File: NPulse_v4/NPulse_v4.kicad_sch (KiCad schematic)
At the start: 48 parts, among them IC1 TXU0202QDCUR, J2 Conn_01x04_Pin, J3 Conn_01x06_Pin, J4 Conn_01x04_Pin, Q1 PMOS, Q2 NMOS, SW1 SW_Push, SW2 SW_SPDT, U1 STM32G484METx, Y1 16MHz

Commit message: some modifications on the routing
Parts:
- H1: footprint MountingHole:MountingHole_3.2mm_M3 -> MountingHole:MountingHole_2.2mm_M2
- IC1: footprint TXU:SOP50P310X90-8N -> TXU0202:SOP50P310X90-8N
- SW1: footprint Button_Switch_SMD:SW_Push_1P1T_NO_CK_KSC7xxJ -> Button_Switch_SMD:SW_SPST_TL3305B
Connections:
- net AD_Vbat: now also U1.17 (PA3); no longer U1.13 (PA1)
- net ENC8_S1: now also U1.12 (PA0); no longer U1.14 (PA2)
- net ENC8_S2: now also U1.13 (PA1); no longer U1.17 (PA3)
- net LED: now also U1.14 (PA2); no longer U1.12 (PA0)
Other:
- note added: "Input"
- note added: "Tactile Button TL3305BF100QG MO: 612-TL3305BF100QG"
- note added: "Translateur TXU0202DCUR DK: 296-TXU0202DCURCT-ND MO: 595-TXU0202DCUR"
- note removed: "Translateur TXU0202DCUR DK: 296-TXU0202DCURCT-ND"
- note removed: "input"

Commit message: Udate mounting holes positions
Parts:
- added H2, H5: MountingHole, MountingHole:MountingHole_2.2mm_M2, symbol Mechanical:MountingHole
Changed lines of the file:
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@@
+	)
+	(symbol
+		(lib_id "Mechanical:MountingHole")
+		(at 129.54 185.42 0)
+		(unit 1)
+		(exclude_from_sim yes)
+		(in_bom no)
+		(on_board yes)
+		(dnp no)
+		(property "Reference" "H5"
+			(at 128.524 189.23 0)
+			(effects
+				(font
+					(size 1.27 1.27)
+				)
+				(justify left)
+			)
+		)
+		(property "Value" "MountingHole"
+			(at 132.08 186.6899 0)
+			(effects
+				(font
+					(size 1.27 1.27)
+				)
+				(justify left)
+				(hide yes)
+			)
+		)
+		(property "Footprint" "MountingHole:MountingHole_2.2mm_M2"
+			(at 129.54 185.42 0)
+			(effects
+				(font
+					(size 1.27 1.27)
+				)
+				(hide yes)
+			)
+		)
+		(property "Datasheet" "~"
+			(at 129.54 185.42 0)
+			(effects
+				(font
+					(size 1.27 1.27)
+				)
+				(hide yes)
+			)
+		)
+		(property "Description" "Mounting Hole without connection"
+			(at 129.54 185.42 0)
+			(effects
+				(font
+					(size 1.27 1.27)
+				)
+				(hide yes)
+			)
+		)
+		(instances
+			(project "NPulse_v4"
+				(path "/1b9ce217-75d5-40c4-b78f-f756c7214a1a"
+					(reference "H5")
+					(unit 1)
+				)
+			)
+		)
 	)
 	(symbol
@@
 					(unit 1)
 				)
+			)
+		)
+	)
+	(symbol
+		(lib_id "Mechanical:MountingHole")
+		(at 121.92 185.42 0)
+		(unit 1)
+		(exclude_from_sim yes)
+		(in_bom no)
+		(on_board yes)
+		(dnp no)
+		(property "Reference" "H2"
+			(at 121.158 189.23 0)
+			(effects
+				(font
+					(size 1.27 1.27)
+				)
+				(justify left)
+			)
+		)
+		(property "Value" "MountingHole"
+			(at 115.062 189.738 0)
+			(effects
+				(font
+					(size 1.27 1.27)
+				)
+				(justify left)
+				(hide yes)
+			)
+		)
+		(property "Footprint" "MountingHole:MountingHole_2.2mm_M2"
+			(at 121.92 185.42 0)
+			(effects
+				(font
+					(size 1.27 1.27)
+				)
+				(hide yes)
+			)
+		)
+		(property "Datasheet" "~"
+			(at 121.92 185.42 0)
+			(effects
+				(font
+					(size 1.27 1.27)
+				)
+				(hide yes)
+			)
+		)
+		(property "Description" "Mounting Hole without connection"
+			(at 121.92 185.42 0)
+			(effects
+				(font
+					(size 1.27 1.27)
+				)
+				(hide yes)
+			)
+		)
+		(instances
+			(project "NPulse_v4"
+				(path "/1b9ce217-75d5-40c4-b78f-f756c7214a1a"
+					(reference "H2")
+					(unit 1)
+				)

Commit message: Correct LDO schematic and update connectors to through-hole footprints
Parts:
- J2, J4: footprint Connector_PinHeader_2.00mm:PinHeader_1x04_P2.00mm_Vertical_SMD_Pin1Left -> Connector_PinHeader_2.00mm:PinHeader_1x04_P2.00mm_Vertical
- J3: footprint Connector_PinHeader_2.54mm:PinHeader_1x06_P2.54mm_Vertical_SMD_Pin1Left -> Connector_PinHeader_2.54mm:PinHeader_1x06_P2.54mm_Vertical
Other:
- note added: "611-PCM12SMTBR"
- note added: "Connecteur 2842102-6 MO: 571-2842102-6"
- note added: "Connector 571-2842102-8 MO: 571-2842102-8"
- note added: "NMOS : VSS138 PMOS : VSS84 DMP2045UQ-7 DMN2053UQ-13"
- note removed: "Connecteur 2842102-4 MO: 571-2842102-4"
- note removed: "Connector HTSW-106-07-FM-S MO: 200-HTSW10607FMS"
- note removed: "NMOS : VSS138 PMOS : VSS84"
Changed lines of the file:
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@@
 		)
 	)
-	(text "NMOS : VSS138\nPMOS : VSS84"
+	(text "NMOS : VSS138\nPMOS : VSS84\n\n DMP2045UQ-7 \n DMN2053UQ-13 "
 		(exclude_from_sim no)
 		(at 247.65 127.254 0)
@@
 		)
 	)
-	(text "Connecteur\n2842102-4\nMO: 571-2842102-4\n"
+	(text "Connecteur\n2842102-6\nMO: 571-2842102-6 \n"
 		(exclude_from_sim no)
 		(at 92.202 189.738 0)
@@
 		)
 	)
+	(text "Connecteur\n2842102-6\nMO: 571-2842102-6\n"
+		(exclude_from_sim no)
+		(at 192.786 79.248 0)
+		(effects
+			(font
+				(size 0.508 0.508)
+			)
+			(justify left)
+		)
+	)
 	(text "4 fils, alim, RX, TX, masse"
 		(exclude_from_sim no)
@@
 		)
 	)
-	(text "Connecteur\n2842102-4\nMO: 571-2842102-4\n"
-		(exclude_from_sim no)
-		(at 191.262 78.994 0)
-		(effects
-			(font
-				(size 0.508 0.508)
-			)
-			(justify left)
-		)
-	)
 	(text "Timers for encoders"
 		(exclude_from_sim no)
@@
 		)
 	)
-	(text "Connector\nHTSW-106-07-FM-S \nMO:  200-HTSW10607FMS "
+	(text " 611-PCM12SMTBR \n"
+		(exclude_from_sim no)
+		(at 198.882 122.682 0)
+		(effects
+			(font
+				(size 1.27 1.27)
+			)
+		)
+	)
+	(text "Connector\n571-2842102-8 \nMO:   571-2842102-8 "
 		(exclude_from_sim no)
 		(at 36.576 145.796 0)
@@
 			)
 		)
-		(property "Footprint" "Connector_PinHeader_2.00mm:PinHeader_1x04_P2.00mm_Vertical_SMD_Pin1Left"
+		(property "Footprint" "Connector_PinHeader_2.00mm:PinHeader_1x04_P2.00mm_Vertical"
 			(at 190.5 86.36 0)
 			(effects
@@
 			)
 		)
-		(property "Footprint" "Connector_PinHeader_2.00mm:PinHeader_1x04_P2.00mm_Vertical_SMD_Pin1Left"
+		(property "Footprint" "Connector_PinHeader_2.00mm:PinHeader_1x04_P2.00mm_Vertical"
 			(at 88.9 185.42 0)
 			(effects
@@
 			)
 		)
-		(property "Footprint" "Connector_PinHeader_2.54mm:PinHeader_1x06_P2.54mm_Vertical_SMD_Pin1Left"
+		(property "Footprint" "Connector_PinHeader_2.54mm:PinHeader_1x06_P2.54mm_Vertical"
 			(at 36.83 134.62 0)
 			(effects

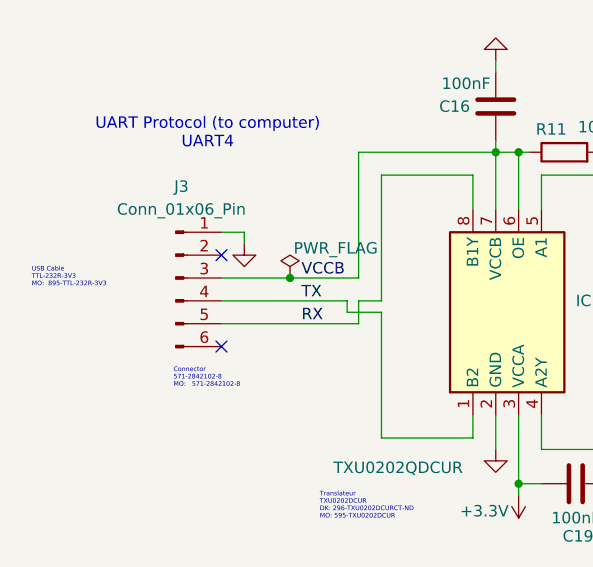
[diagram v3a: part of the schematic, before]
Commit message: convert pin headers to 2.54mm
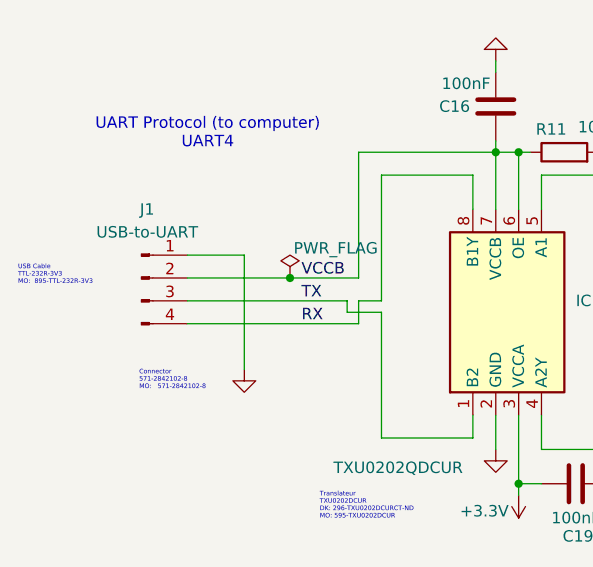
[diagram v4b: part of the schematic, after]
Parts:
- removed J3: Conn_01x06_Pin, Connector_PinHeader_2.54mm:PinHeader_1x06_P2.54mm_Vertical, symbol Connector:Conn_01x06_Pin
- added J1: USB-to-UART, Connector_PinHeader_2.54mm:PinHeader_1x04_P2.54mm_Vertical, symbol Connector:Conn_01x04_Pin
- J2: footprint Connector_PinHeader_2.00mm:PinHeader_1x04_P2.00mm_Vertical -> Connector_PinHeader_2.54mm:PinHeader_1x04_P2.54mm_Vertical
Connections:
- net GND: now also J1.1 (Pin_1)
- net RX: now also J1.4 (Pin_4)
- net TX: now also J1.3 (Pin_3)
- net VCCB: now also J1.2 (Pin_2)
- no-connect marks 5 -> 3
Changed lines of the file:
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@@
 	(text "USB Cable\nTTL-232R-3V3 \nMO:  895-TTL-232R-3V3 "
 		(exclude_from_sim no)
-		(at 20.828 134.62 0)
+		(at 19.304 134.366 0)
 		(effects
 			(font
@@
 	(text "Connector\n571-2842102-8 \nMO:   571-2842102-8 "
 		(exclude_from_sim no)
-		(at 36.576 145.796 0)
+		(at 32.766 146.05 0)
 		(effects
 			(font
@@
 	)
 	(no_connect
-		(at 41.91 142.24)
-	)
-	(no_connect
 		(at 158.75 119.38)
 	)
@@
 		(at 120.65 68.58)
 	)
-	(no_connect
-		(at 41.91 132.08)
-	)
 	(wire
 		(pts
@@
 	(wire
 		(pts
-			(xy 115.57 71.12) (xy 120.65 71.12)
+			(xy 38.1 132.08) (xy 44.45 132.08)
 		)
 		(stroke
@@
 	(wire
 		(pts
-			(xy 247.65 96.52) (xy 251.46 96.52)
+			(xy 115.57 71.12) (xy 120.65 71.12)
 		)
 		(stroke
@@
 	(wire
 		(pts
-			(xy 41.91 134.62) (xy 49.53 134.62)
+			(xy 247.65 96.52) (xy 251.46 96.52)
 		)
 		(stroke
@@
 	(wire
 		(pts
-			(xy 41.91 139.7) (xy 57.15 139.7)
+			(xy 133.35 43.18) (xy 135.89 43.18)
 		)
 		(stroke
@@
 	(wire
 		(pts
-			(xy 133.35 43.18) (xy 135.89 43.18)
+			(xy 247.65 86.36) (xy 247.65 87.63)
 		)
 		(stroke
@@
 	(wire
 		(pts
-			(xy 247.65 86.36) (xy 247.65 87.63)
+			(xy 38.1 139.7) (xy 57.15 139.7)
 		)
 		(stroke
@@
 	(wire
 		(pts
-			(xy 259.08 91.44) (xy 259.08 86.36)
+			(xy 38.1 134.62) (xy 49.53 134.62)
 		)
 		(stroke
@@
 	(wire
 		(pts
-			(xy 71.12 85.09) (xy 81.28 85.09)
+			(xy 259.08 91.44) (xy 259.08 86.36)
 		)
 		(stroke
@@
 	(wire
 		(pts
-			(xy 269.24 142.24) (xy 269.24 140.97)
+			(xy 71.12 85.09) (xy 81.28 85.09)
 		)
 		(stroke
@@
 	(wire
 		(pts
-			(xy 62.23 35.56) (xy 62.23 34.29)
+			(xy 269.24 142.24) (xy 269.24 140.97)
 		)
 		(stroke
@@
 	(wire
 		(pts
-			(xy 269.24 123.19) (xy 269.24 124.46)
+			(xy 62.23 35.56) (xy 62.23 34.29)
 		)
 		(stroke
@@
 	(wire
 		(pts
-			(xy 166.37 34.29) (xy 166.37 35.56)
+			(xy 269.24 123.19) (xy 269.24 124.46)
 		)
 		(stroke
@@
 	(wire
 		(pts
-			(xy 62.23 55.88) (xy 62.23 57.15)
+			(xy 166.37 34.29) (xy 166.37 35.56)
 		)
 		(stroke
@@
 	(wire
 		(pts
-			(xy 41.91 137.16) (xy 55.88 137.16)
+			(xy 62.23 55.88) (xy 62.23 57.15)
 		)
 		(stroke
@@
 	(wire
 		(pts
-			(xy 44.45 129.54) (xy 44.45 130.81)
+			(xy 44.45 132.08) (xy 44.45 144.78)
 		)
 		(stroke
@@
 	(wire
 		(pts
+			(xy 38.1 137.16) (xy 55.88 137.16)
+		)
+		(stroke
+			(width 0)
+			(type default)
+		)
+	)
+	(wire
+		(pts
 			(xy 158.75 66.04) (xy 167.64 66.04)
 		)
@@
 	(wire
 		(pts
-			(xy 41.91 129.54) (xy 44.45 129.54)
-		)
-		(stroke
-			(width 0)
-			(type default)
-		)
-	)
-	(wire
-		(pts
 			(xy 260.35 140.97) (xy 260.35 142.24)
 		)
@@
 	(symbol
 		(lib_id "power:GND")
-		(at 44.45 130.81 0)
+		(at 44.45 144.78 0)
 		(unit 1)
 		(exclude_from_sim no)
@@
 		(fields_autoplaced yes)
 		(property "Reference" "#PWR020"
-			(at 44.45 137.16 0)
+			(at 44.45 151.13 0)
 			(effects
 				(font
@@
 		)
 		(property "Value" "GND"
-			(at 44.45 135.89 0)
+			(at 44.45 149.86 0)
 			(effects
 				(font
@@
 		)
 		(property "Footprint" ""
-			(at 44.45 130.81 0)
+			(at 44.45 144.78 0)
 			(effects
 				(font
@@
 		)
 		(property "Datasheet" ""
-			(at 44.45 130.81 0)
+			(at 44.45 144.78 0)
 			(effects
 				(font
@@
 		)
 		(property "Description" "Power symbol creates a global label with name \"GND\" , ground"
-			(at 44.45 130.81 0)
+			(at 44.45 144.78 0)
 			(effects
 				(font
@@
 			)
 		)
-		(property "Footprint" "Connector_PinHeader_2.00mm:PinHeader_1x04_P2.00mm_Vertical"
+		(property "Footprint" "Connector_PinHeader_2.54mm:PinHeader_1x04_P2.54mm_Vertical"
 			(at 190.5 86.36 0)
 			(effects
@@
 	)
 	(symbol
-		(lib_id "power:GND")
-		(at 82.55 189.23 0)
+		(lib_id "Connector:Conn_01x04_Pin")
+		(at 33.02 134.62 0)
 		(unit 1)
 		(exclude_from_sim no)
@@
 		(dnp no)
 		(fields_autoplaced yes)
-		(property "Reference" "#PWR030"
-			(at 82.55 195.58 0)
+		(property "Reference" "J1"
+			(at 33.655 127 0)
 			(effects
 				(font
 					(size 1.27 1.27)
 				)
-				(hide yes)
 			)
 		)
-		(property "Value" "GND"
-			(at 82.55 194.31 0)
+		(property "Value" "USB-to-UART"
+			(at 33.655 129.54 0)
 			(effects
 				(font
 					(size 1.27 1.27)
 				)
-				(hide yes)
 			)
 		)
-		(property "Footprint" ""
-			(at 82.55 189.23 0)
+		(property "Footprint" "Connector_PinHeader_2.54mm:PinHeader_1x04_P2.54mm_Vertical"
+			(at 33.02 134.62 0)
 			(effects
 				(font
@@
 			)
 		)
-		(property "Datasheet" ""
-			(at 82.55 189.23 0)
+		(property "Datasheet" "~"
+			(at 33.02 134.62 0)
 			(effects
 				(font
@@
 			)
 		)
-		(property "Description" "Power symbol creates a global label with name \"GND\" , ground"
-			(at 82.55 189.23 0)
+		(property "Description" "Generic connector, single row, 01x04, script generated"
+			(at 33.02 134.62 0)
 			(effects
 				(font
@@
 		(pin "1"
 		)
+		(pin "2"
+		)
+		(pin "3"
+		)
+		(pin "4"
+		)
 		(instances
-			(project "NPulse_v4"
+			(project ""
 				(path "/1b9ce217-75d5-40c4-b78f-f756c7214a1a"
-					(reference "#PWR030")
+					(reference "J1")
 					(unit 1)
 				)
@@
 	)
 	(symbol
-		(lib_id "Connector:Conn_01x06_Pin")
-		(at 36.83 134.62 0)
+		(lib_id "power:GND")
+		(at 82.55 189.23 0)
 		(unit 1)
 		(exclude_from_sim no)
@@
 		(dnp no)
 		(fields_autoplaced yes)
-		(property "Reference" "J3"
-			(at 37.465 124.46 0)
+		(property "Reference" "#PWR030"
+			(at 82.55 195.58 0)
 			(effects
 				(font
 					(size 1.27 1.27)
 				)
+				(hide yes)
 			)
 		)
-		(property "Value" "Conn_01x06_Pin"
-			(at 37.465 127 0)
+		(property "Value" "GND"
+			(at 82.55 194.31 0)
 			(effects
 				(font
 					(size 1.27 1.27)
 				)
+				(hide yes)
 			)
 		)
-		(property "Footprint" "Connector_PinHeader_2.54mm:PinHeader_1x06_P2.54mm_Vertical"
-			(at 36.83 134.62 0)
+		(property "Footprint" ""
+			(at 82.55 189.23 0)
 			(effects
 				(font
@@
 			)
 		)
-		(property "Datasheet" "~"
-			(at 36.83 134.62 0)
+		(property "Datasheet" ""
+			(at 82.55 189.23 0)
 			(effects
 				(font
@@
 			)
 		)
-		(property "Description" "Generic connector, single row, 01x06, script generated"
-			(at 36.83 134.62 0)
+		(property "Description" "Power symbol creates a global label with name \"GND\" , ground"
+			(at 82.55 189.23 0)
 			(effects
 				(font
@@
 		(pin "1"
 		)
-		(pin "2"
-		)
-		(pin "3"
-		)
-		(pin "6"
-		)
-		(pin "4"
-		)
-		(pin "5"
-		)
 		(instances
 			(project "NPulse_v4"
 				(path "/1b9ce217-75d5-40c4-b78f-f756c7214a1a"
-					(reference "J3")
+					(reference "#PWR030")
 					(unit 1)
 				)

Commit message: add license
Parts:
- J4: footprint Connector_PinHeader_2.00mm:PinHeader_1x04_P2.00mm_Vertical -> Connector_PinHeader_2.54mm:PinHeader_1x04_P2.54mm_Vertical
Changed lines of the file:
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@@
 			)
 		)
-		(property "Footprint" "Connector_PinHeader_2.00mm:PinHeader_1x04_P2.00mm_Vertical"
+		(property "Footprint" "Connector_PinHeader_2.54mm:PinHeader_1x04_P2.54mm_Vertical"
 			(at 88.9 185.42 0)
 			(effects
